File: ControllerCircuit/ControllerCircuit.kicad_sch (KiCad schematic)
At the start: 88 parts, among them J1 ScrewTerminal, J10 ESTOP, J12 ScrewTerminal, J14 Unused header, J15 Molex 0472192001, J2 ScrewTerminal3Pin, J3 ScrewTerminal3Pin, J4 ScrewTerminal, J5 ScrewTerminal, J7 ScrewTerminal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

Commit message: Fixed JLCPCB part number #170
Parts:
- U12, U9: LCSCStockCode C250827 -> C2691601
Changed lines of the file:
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@@
       (effects (font (size 1.27 1.27)) (justify left) hide)
     )
-    (property "LCSCStockCode" "C250827" (at 179.07 145.796 0)
+    (property "LCSCStockCode" "C2691601" (at 179.07 145.796 0)
       (effects (font (size 1.27 1.27)) hide)
     )
@@
       (effects (font (size 1.27 1.27)) (justify left) hide)
     )
-    (property "LCSCStockCode" "C250827" (at 180.975 167.132 0)
-      (effects (font (size 1.27 1.27)) hide)
-    )
+    (property "LCSCStockCode" "C2691601" (at 180.975 167.132 0)
+      (effects (font (size 1.27 1.27)) hide)
+    )

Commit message: Added 4 female pin headers to BOM/placement
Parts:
- added J11, J6: 19PinSocket, symbol Connector:Conn_01x19_Socket
- added J13: 14PinSocket, symbol Connector:Conn_01x14_Socket
- added J16: 4PinSocket, symbol Connector:Conn_01x04_Socket
- J9: value Shunt -> ScrewTerminal
- LCD1: LCSCStockCode C52711/C358718 -> (none)
- U4: LCSCStockCode C319202/C319202 -> (none)
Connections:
- net at J2.1 (Pin_1), K1.COM: now also J2.2 (Pin_2), J2.3 (Pin_3), K1.NC, K1.NO
- net at J3.1 (Pin_1), K2.COM: now also J3.2 (Pin_2), J3.3 (Pin_3), K2.NC, K2.NO
- net at U9.3: now also J12.2 (Pin_2); no longer J12.1 (Pin_1)
- net at U9.4: now also J12.1 (Pin_1); no longer J12.2 (Pin_2)
- net at J12.3 (Pin_3), U12.3: now also J12.4 (Pin_4), U12.4
- no-connect marks 16 -> 72
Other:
- note added: "Connectors are only here to provide BOM and footprints for PCB"
- note added: "LT219-1 60V AC/DC + 1Amp"
- note removed: "Panasonic AQY282SX Solid State Relay 60V 500mA AC or DC"
- moved on the sheet: C10, C11, C5, C7, D1, D2, D3, D4, D5, J12, J15, J2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

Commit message: Connectors to plug terminal blocks WJ15EDGRC-3.81
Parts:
- removed RX1: Receive, Connector_JST:JST_PH_S2B-PH-K_1x02_P2.00mm_Horizontal, symbol ControllerCircuit-rescue:Conn_01x02_Male-Connector
- removed TX1: Transmit, Connector_JST:JST_PH_S2B-PH-K_1x02_P2.00mm_Horizontal, symbol ControllerCircuit-rescue:Conn_01x02_Male-Connector
- added J17: 4PinBlock, ControllerCircuit:WJ15EDGRC-3.81-4P, symbol ControllerCircuit-rescue:Conn_01x04_Female-Connector
- D2, D5: LCSCStockCode C9808 -> C181117
- J1, J12, J4, J7, J9: value ScrewTerminal -> 4PinBlock; footprint ControllerCircuit:Terminal-Block_3.81_4P_LCSC_C395880 -> ControllerCircuit:WJ15EDGRC-3.81-4P
- J5: LCSCStockCode C395878 -> C8387; Manufacturer_Part_Number (none) -> WJ15EDGRC-3.81-2P
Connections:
- net GND: now also J17.1 (Pin_1)
- net at U2.3: now also J17.3 (Pin_3)
- net at U2.4: now also J17.4 (Pin_4)
- net at Q4.1 (G), R2.1: now also J17.2 (Pin_2)
- net at U9.3: now also J12.1 (Pin_1); no longer J12.2 (Pin_2)
- net at U9.4: now also J12.2 (Pin_2); no longer J12.1 (Pin_1)
- net at J12.3 (Pin_3), U12.3: no longer J12.4 (Pin_4), U12.4
- new net: J2.1 (Pin_1), K1.COM
- new net: J2.2 (Pin_2), K1.NC
- new net: J2.3 (Pin_3), K1.NO
- new net: J3.1 (Pin_1), K2.COM
- new net: J3.2 (Pin_2), K2.NC
- new net: J3.3 (Pin_3), K2.NO
- new net: J12.4 (Pin_4), U12.4
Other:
- moved on the sheet: C5, C8, C9, J12, J2, J3, Q4, R20, R3, R32, U2

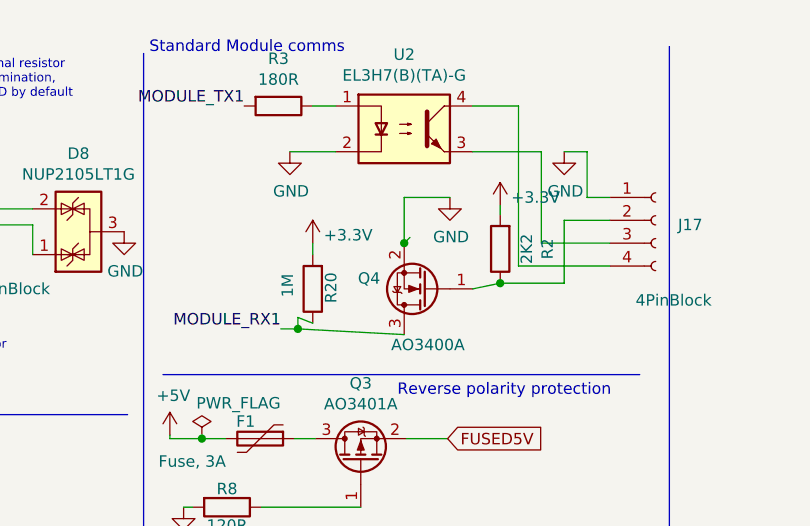
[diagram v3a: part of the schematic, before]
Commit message: Swap parts to 0603 to ease order/build
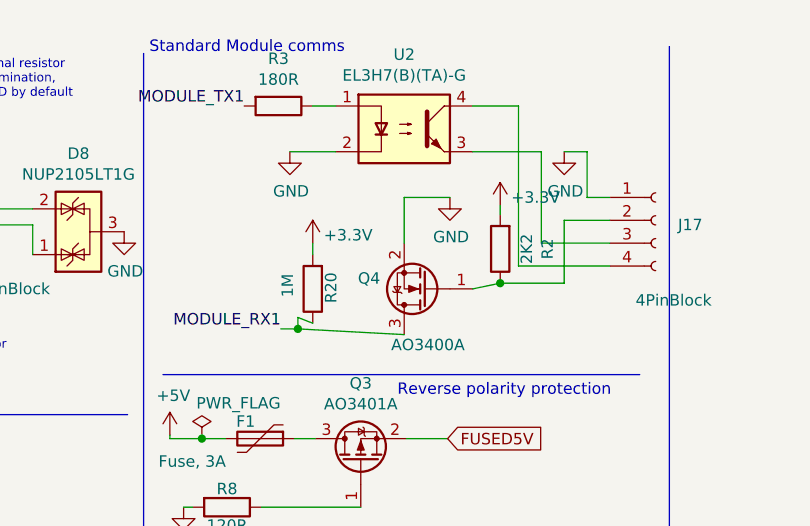
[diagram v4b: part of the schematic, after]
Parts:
- C1, C2, C6, C8, C9: footprint Capacitor_SMD:C_0805_2012Metric -> Capacitor_SMD:C_0603_1608Metric; LCSCStockCode C49678 -> C14663; PartNumber (none) -> CC0603KRX7R9BB104
- C10, C13: footprint Capacitor_SMD:C_0805_2012Metric -> Capacitor_SMD:C_0603_1608Metric; LCSCStockCode C28323 -> C15849; PartNumber CL21B105KBFNNNE -> CL10A105KB8NNNC
- C11, C7: footprint Capacitor_SMD:C_0805_2012Metric -> Capacitor_SMD:C_0603_1608Metric; LCSCStockCode C28323 -> C15849; PartNumber (none) -> CL10A105KB8NNNC
- C14: footprint Capacitor_SMD:C_0805_2012Metric -> Capacitor_SMD:C_0603_1608Metric; LCSCStockCode C49678 -> C14663; PartNumber CC0805KRX7R9BB104 -> CC0603KRX7R9BB104
- J5: footprint ControllerCircuit:Terminal-Block_3.81_2P-LCSC_C395878 -> ControllerCircuit:WJ15EDGRC-3.81-2P
- R1, R17, R18, R21, R25: footprint Resistor_SMD:R_0805_2012Metric -> Resistor_SMD:R_0603_1608Metric; LCSCStockCode C17557 -> C22962; PartNumber 0805W8F2200T5E -> 0603WAF2200T5E
- R10, R12, R13, R14, R4: footprint Resistor_SMD:R_0805_2012Metric -> Resistor_SMD:R_0603_1608Metric; LCSCStockCode C28636 -> C23204; PartNumber 0805W8F5600T5E -> 0603WAF5600T5E
- R11, R15, R27, R7: footprint Resistor_SMD:R_0805_2012Metric -> Resistor_SMD:R_0603_1608Metric; LCSCStockCode C17737 -> C23196; PartNumber 0805W8F5102T5E -> 0603WAF5102T5E
- R16, R2, R5: footprint Resistor_SMD:R_0805_2012Metric -> Resistor_SMD:R_0603_1608Metric; LCSCStockCode C17520 -> C4190; PartNumber 0805W8F2201T5E -> 0603WAF2201T5E
- R19, R22, R29, R31, R32: footprint Resistor_SMD:R_0805_2012Metric -> Resistor_SMD:R_0603_1608Metric; LCSCStockCode C17414 -> C25804; PartNumber 0805W8F1002T5E -> 0603WAF1002T5E
- R20: footprint Resistor_SMD:R_0805_2012Metric -> Resistor_SMD:R_0603_1608Metric; LCSCStockCode C17514 -> C22935; PartNumber 0805W8F1004T5E -> 0603WAF1004T5E
- R24, R26, R28: footprint Resistor_SMD:R_0805_2012Metric -> Resistor_SMD:R_0603_1608Metric; LCSCStockCode C17560 -> C31850; PartNumber 0805W8F2202T5E -> 0603WAF2202T5E
- R6, R8, R9: footprint Resistor_SMD:R_0805_2012Metric -> Resistor_SMD:R_0603_1608Metric; LCSCStockCode C17437 -> C22787; PartNumber 0805W8F1200T5E -> 0603WAF1200T5E

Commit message: Tidy up part numbers
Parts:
- J1, J12, J17, J4, J7, J9: LCSCStockCode C395880 -> C7245
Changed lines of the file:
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@@
       (effects (font (size 1.27 1.27)) hide)
     )
-    (property "LCSCStockCode" "C395880" (at 116.586 38.989 0)
+    (property "LCSCStockCode" "C7245" (at 116.586 38.989 0)
       (effects (font (size 1.27 1.27)) hide)
     )
@@
       (effects (font (size 1.27 1.27)) hide)
     )
-    (property "LCSCStockCode" "C395880" (at 325.12 154.94 0)
+    (property "LCSCStockCode" "C7245" (at 325.12 154.94 0)
       (effects (font (size 1.27 1.27)) hide)
     )
@@
       (effects (font (size 1.27 1.27)) hide)
     )
-    (property "LCSCStockCode" "C395880" (at 61.976 108.712 0)
+    (property "LCSCStockCode" "C7245" (at 61.976 108.712 0)
       (effects (font (size 1.27 1.27)) hide)
     )
@@
       (effects (font (size 1.27 1.27)) hide)
     )
-    (property "LCSCStockCode" "C395880" (at 200.66 162.56 0)
+    (property "LCSCStockCode" "C7245" (at 200.66 162.56 0)
       (effects (font (size 1.27 1.27)) hide)
     )
@@
       (effects (font (size 1.27 1.27)) hide)
     )
-    (property "LCSCStockCode" "C395880" (at 152.781 216.408 0)
+    (property "LCSCStockCode" "C7245" (at 152.781 216.408 0)
       (effects (font (size 1.27 1.27)) hide)
     )
@@
       (effects (font (size 1.27 1.27)) hide)
     )
-    (property "LCSCStockCode" "C395880" (at 193.04 33.02 0)
+    (property "LCSCStockCode" "C7245" (at 193.04 33.02 0)
       (effects (font (size 1.27 1.27)) hide)
     )

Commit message: Silkscreen
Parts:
- U1: JLCPCBRotation (none) -> 180
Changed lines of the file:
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@@
+      (effects (font (size 1.27 1.27)) hide)
+    )
+    (property "JLCPCBRotation" "180" (at 38.1 35.56 0)
       (effects (font (size 1.27 1.27)) hide)
     )
